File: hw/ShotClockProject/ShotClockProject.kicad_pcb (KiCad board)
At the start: 2 copper layers, 94 parts, among them IC1 TP4056-42-ESOP8_Rearanged, J1 USB_C_Receptacle_USB2.0, J10 Conn_01x33_Pin, J2 Conn_ST_STDC14, J3 Conn_01x06_Pin, J4 Conn_01x03_Pin, J5 Conn_01x02_Pin, J6 Conn_01x03_Pin, J7 Conn_01x33_Pin, J8 Conn_01x33_Pin, J9 Conn_01x33_Pin, Q1 Q_NPN_BCE, Q2 Q_PMOS_SGD, SW1 SW_SPDT, SW2 SW_SPDT, SW3 SW_SPST, SW4 SW_SPST, SW5 SW_SPST, U1 STM32F103RCT6, U2 LD39015M33R, U3 TPS63000, U4 M74HC14YRM13TR, Y1 16MHz

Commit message: Changed footprint
To horizontal 2.54 connectors
and started on rough layout
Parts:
- C10, C11, C12, C13, C15, C17, C2, C21, C22, C23, C24, C3, C4, C5, C6, C7, C8, C9: footprint Capacitor_SMD:C_0603_1608Metric -> Capacitor_SMD:C_0402_1005Metric
- J2: footprint Connector_PinHeader_1.27mm:PinHeader_2x07_P1.27mm_Vertical_SMD -> Connector_PinHeader_1.27mm:PinHeader_2x07_P1.27mm_Horizontal
- J3: footprint Connector_PinHeader_2.54mm:PinHeader_1x06_P2.54mm_Vertical_SMD_Pin1Left -> Connector_PinHeader_2.54mm:PinHeader_1x06_P2.54mm_Horizontal
- J4: footprint Connector_PinHeader_1.00mm:PinHeader_1x03_P1.00mm_Vertical_SMD_Pin1Left -> Connector_PinHeader_1.00mm:PinHeader_1x03_P1.00mm_Horizontal
- J5: footprint Connector_PinHeader_2.54mm:PinHeader_1x02_P2.54mm_Vertical_SMD_Pin1Left -> Connector_PinHeader_2.54mm:PinHeader_1x02_P2.54mm_Horizontal
- J6: footprint Connector_PinHeader_2.54mm:PinHeader_1x03_P2.54mm_Vertical_SMD_Pin1Left -> Connector_PinHeader_2.54mm:PinHeader_1x03_P2.54mm_Horizontal
- R1, R10, R11, R12, R13, R14, R15, R16, R17, R18, R19, R2, R20, R21, R22, R23, R24, R25, R26, R27, R3, R4, R5, R6, R7, R8, R9: footprint Resistor_SMD:R_0603_1608Metric -> Resistor_SMD:R_0402_1005Metric
- moved J9 121.1 mm to (186.8, 156.8), turned to -90 degrees
- moved J10 111.9 mm to (100.8, 152.5), turned to 180 degrees
- moved Y1 111.3 mm to (134.3, 93.7)
- moved C10 110.3 mm to (137.2, 93.1), turned to 90 degrees
- moved C11 110.2 mm to (137.2, 95.1), turned to 90 degrees
- moved C7 108.6 mm to (139.7, 97.5)
- moved C2 108.4 mm to (143.9, 88.0)
- moved FB1 108.2 mm to (138.2, 103.8)
- moved J1 108.1 mm to (168.9, 94.9)
- moved R3 108.1 mm to (161.9, 96.5)
- moved R5 108.1 mm to (161.9, 98.5)
- moved R6 108.1 mm to (161.7, 93.5)
- moved U1 108.1 mm to (147.5, 95.6)
- moved C4 107.9 mm to (144.5, 103.5)
- moved C5 107.4 mm to (151.2, 103.5)
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
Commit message: Added manufacturer folders
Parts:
- moved R1 153.5 mm to (125.5, 78.8), turned to 90 degrees
- moved IC1 144.8 mm to (118.2, 124.2), turned to 90 degrees
- moved R4 131.5 mm to (145.8, 87.5), turned to -90 degrees
- moved SW2 124.0 mm to (146.0, 82.5), turned to 180 degrees
- moved Q2 120.5 mm to (151.7, 113.2), turned to -90 degrees
- moved R11 104.0 mm to (158.2, 98.0)
- moved J2 63.4 mm to (158.2, 77.4), turned to 0 degrees
- moved J3 28.1 mm to (169.8, 104.8)
- moved SW1 13.2 mm to (126.2, 73.5)

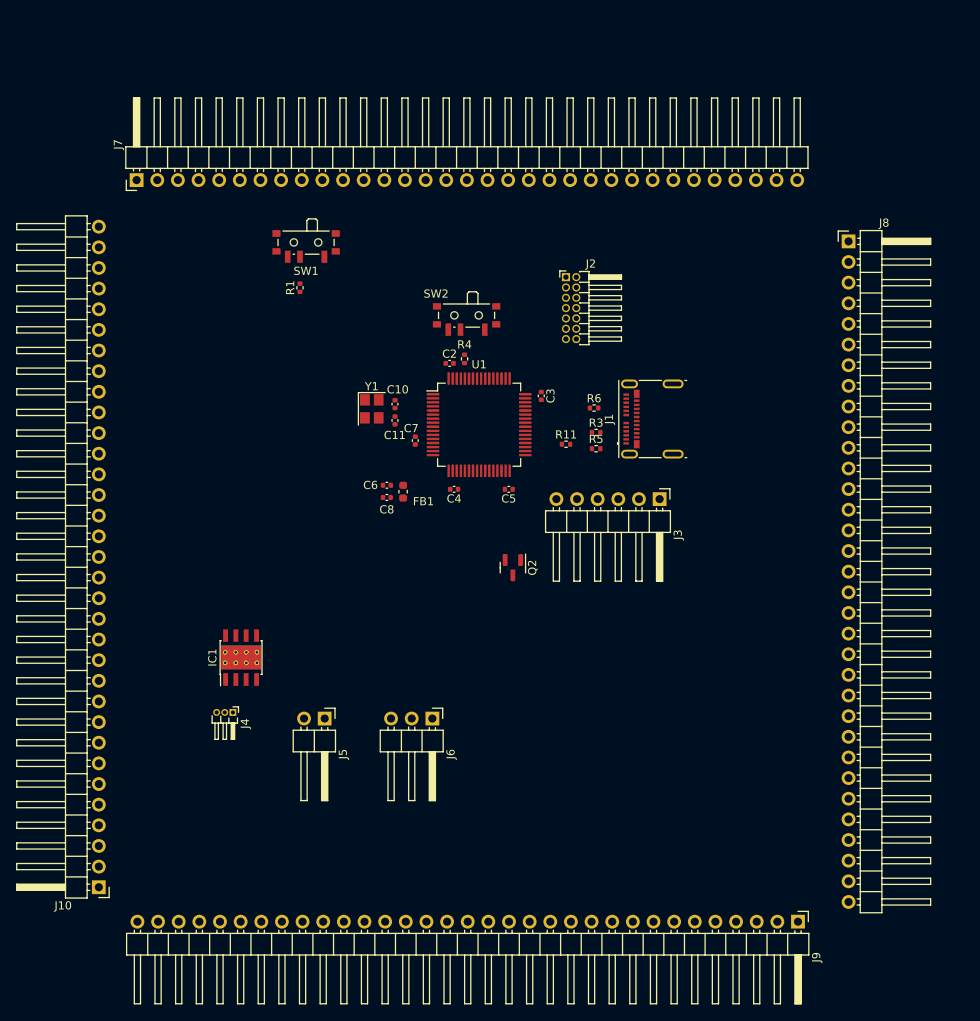
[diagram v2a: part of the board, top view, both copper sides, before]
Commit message: Changes headers, usb schematic and footprint
Now using standing USBc
Header & header pins are imported
All have 3d models now.

Removed fp-info-cache and added it to gitignore
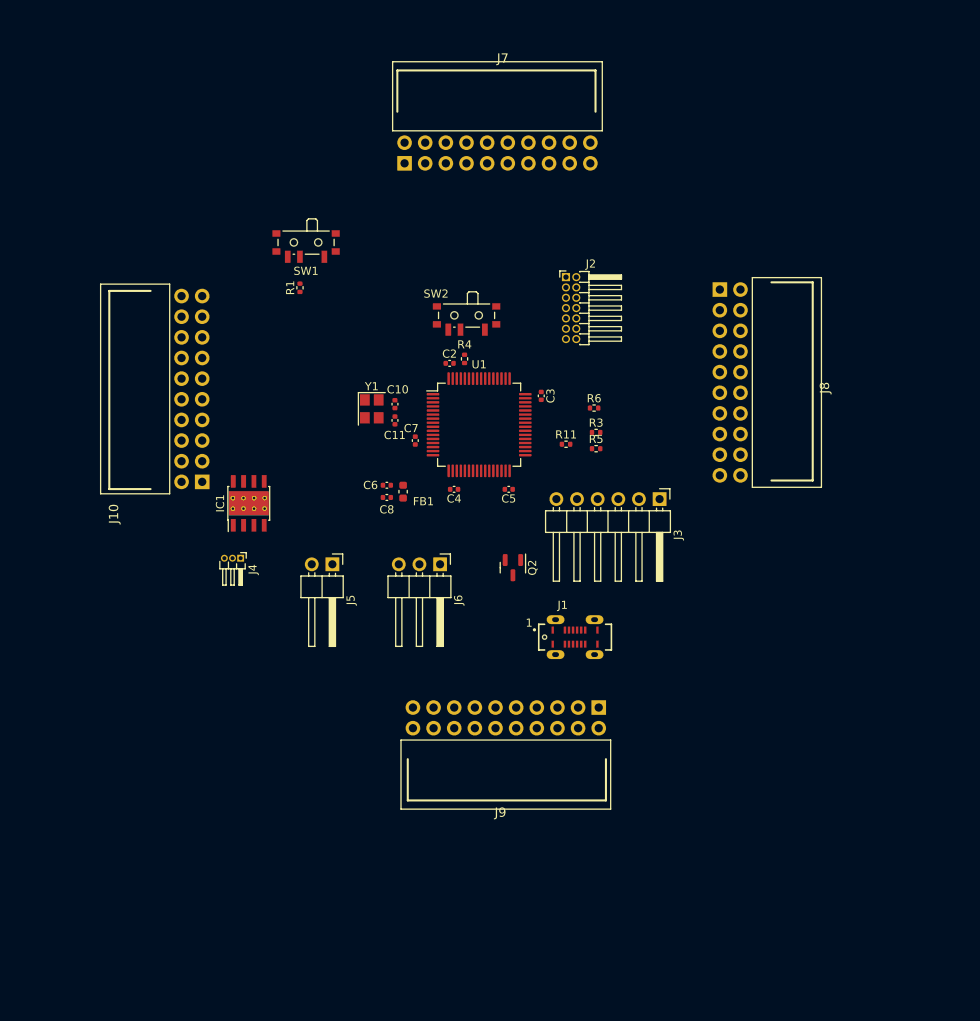
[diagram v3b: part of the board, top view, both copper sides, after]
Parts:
- J1: value USB_C_Receptacle_USB2.0 -> USB4120-03-C_REVA; footprint Connector_USB:USB_C_Receptacle_Molex_105450-0101 -> USB4120-03-C:GCT_USB4120-03-C_REVA_With3DModel
- J10, J7, J8, J9: value Conn_01x33_Pin -> DW254W-22-20-85; footprint Connector_PinHeader_2.54mm:PinHeader_1x33_P2.54mm_Horizontal -> DW254W-22-20-85:CONN-TH_20P-P2.54_DEALON_DW254W-22-20-85
- moved J10 62.4 mm to (112.2, 91.2), turned to 90 degrees
- moved J7 44.5 mm to (149.8, 62.2), turned to 0 degrees
- moved J9 43.8 mm to (150.8, 131.7), turned to 180 degrees
- moved J1 28.5 mm to (159.3, 121.7), turned to 0 degrees
- moved J8 22.7 mm to (178.4, 90.4), turned to -90 degrees
- moved IC1 19.0 mm to (119.2, 105.3)
- moved J4 19.0 mm to (118.2, 112.0)
- moved J5 19.0 mm to (129.5, 112.8)
- moved J6 19.0 mm to (142.7, 112.8)
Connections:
- J10 pad 10: /Connectors to segment displays/PWM5_TIM3_CH1 -> /Connectors to segment displays/PWM12_TIM4_CH4
- J10 pad 11: GND -> /Connectors to segment displays/PWM5_TIM3_CH1
- J10 pad 12: /Connectors to segment displays/PWM6_TIM3_CH2 -> /Connectors to segment displays/PWM13_TIM5_CH1
- J10 pad 13: GND -> /Connectors to segment displays/PWM6_TIM3_CH2
- J10 pad 14: /Connectors to segment displays/PWM7_TIM3_CH3 -> /Connectors to segment displays/PWM14_TIM5_CH2
- J10 pad 15: GND -> /Connectors to segment displays/PWM7_TIM3_CH3
- J10 pad 16: /Connectors to segment displays/PWM8_TIM3_CH4 -> /Connectors to segment displays/PWM15_TIM5_CH3
- J10 pad 17: GND -> /Connectors to segment displays/PWM8_TIM3_CH4
- J10 pad 18: /Connectors to segment displays/PWM9_TIM4_CH1 -> /Connectors to segment displays/PWM16_TIM5_CH4
- J10 pad 2: /Connectors to segment displays/PWM1_TIM2_CH1 -> GND
- J10 pad 20: /Connectors to segment displays/PWM10_TIM4_CH2 -> GND
- J10 pad 3: GND -> /Connectors to segment displays/PWM1_TIM2_CH1
- J10 pad 4: /Connectors to segment displays/PWM2_TIM2_CH2 -> /Connectors to segment displays/PWM9_TIM4_CH1
- J10 pad 5: GND -> /Connectors to segment displays/PWM2_TIM2_CH2
- J10 pad 6: /Connectors to segment displays/PWM3_TIM2_CH3 -> /Connectors to segment displays/PWM10_TIM4_CH2
- J10 pad 7: GND -> /Connectors to segment displays/PWM3_TIM2_CH3
- J10 pad 8: /Connectors to segment displays/PWM4_TIM2_CH4 -> /Connectors to segment displays/PWM11_TIM4_CH3
- J10 pad 9: GND -> /Connectors to segment displays/PWM4_TIM2_CH4
- J7 pad 10: /Connectors to segment displays/PWM5_TIM3_CH1 -> /Connectors to segment displays/PWM12_TIM4_CH4
- J7 pad 11: GND -> /Connectors to segment displays/PWM5_TIM3_CH1
- J7 pad 12: /Connectors to segment displays/PWM6_TIM3_CH2 -> /Connectors to segment displays/PWM13_TIM5_CH1
- J7 pad 13: GND -> /Connectors to segment displays/PWM6_TIM3_CH2
- J7 pad 14: /Connectors to segment displays/PWM7_TIM3_CH3 -> /Connectors to segment displays/PWM14_TIM5_CH2
- J7 pad 15: GND -> /Connectors to segment displays/PWM7_TIM3_CH3
- J7 pad 16: /Connectors to segment displays/PWM8_TIM3_CH4 -> /Connectors to segment displays/PWM15_TIM5_CH3
- J7 pad 17: GND -> /Connectors to segment displays/PWM8_TIM3_CH4
- J7 pad 18: /Connectors to segment displays/PWM9_TIM4_CH1 -> /Connectors to segment displays/PWM16_TIM5_CH4
- J7 pad 2: /Connectors to segment displays/PWM1_TIM2_CH1 -> GND
- J7 pad 20: /Connectors to segment displays/PWM10_TIM4_CH2 -> GND
- J7 pad 3: GND -> /Connectors to segment displays/PWM1_TIM2_CH1
- J7 pad 4: /Connectors to segment displays/PWM2_TIM2_CH2 -> /Connectors to segment displays/PWM9_TIM4_CH1
- J7 pad 5: GND -> /Connectors to segment displays/PWM2_TIM2_CH2
- J7 pad 6: /Connectors to segment displays/PWM3_TIM2_CH3 -> /Connectors to segment displays/PWM10_TIM4_CH2
- J7 pad 7: GND -> /Connectors to segment displays/PWM3_TIM2_CH3
- J7 pad 8: /Connectors to segment displays/PWM4_TIM2_CH4 -> /Connectors to segment displays/PWM11_TIM4_CH3
- J7 pad 9: GND -> /Connectors to segment displays/PWM4_TIM2_CH4
- J8 pad 10: /Connectors to segment displays/PWM5_TIM3_CH1 -> /Connectors to segment displays/PWM12_TIM4_CH4
- J8 pad 11: GND -> /Connectors to segment displays/PWM5_TIM3_CH1
- J8 pad 12: /Connectors to segment displays/PWM6_TIM3_CH2 -> /Connectors to segment displays/PWM13_TIM5_CH1
- J8 pad 13: GND -> /Connectors to segment displays/PWM6_TIM3_CH2
- J8 pad 14: /Connectors to segment displays/PWM7_TIM3_CH3 -> /Connectors to segment displays/PWM14_TIM5_CH2
- J8 pad 15: GND -> /Connectors to segment displays/PWM7_TIM3_CH3
- J8 pad 16: /Connectors to segment displays/PWM8_TIM3_CH4 -> /Connectors to segment displays/PWM15_TIM5_CH3
- J8 pad 17: GND -> /Connectors to segment displays/PWM8_TIM3_CH4
- J8 pad 18: /Connectors to segment displays/PWM9_TIM4_CH1 -> /Connectors to segment displays/PWM16_TIM5_CH4
- J8 pad 2: /Connectors to segment displays/PWM1_TIM2_CH1 -> GND
- J8 pad 20: /Connectors to segment displays/PWM10_TIM4_CH2 -> GND
- J8 pad 3: GND -> /Connectors to segment displays/PWM1_TIM2_CH1
- J8 pad 4: /Connectors to segment displays/PWM2_TIM2_CH2 -> /Connectors to segment displays/PWM9_TIM4_CH1
- J8 pad 5: GND -> /Connectors to segment displays/PWM2_TIM2_CH2
- J8 pad 6: /Connectors to segment displays/PWM3_TIM2_CH3 -> /Connectors to segment displays/PWM10_TIM4_CH2
- J8 pad 7: GND -> /Connectors to segment displays/PWM3_TIM2_CH3
- J8 pad 8: /Connectors to segment displays/PWM4_TIM2_CH4 -> /Connectors to segment displays/PWM11_TIM4_CH3
- J8 pad 9: GND -> /Connectors to segment displays/PWM4_TIM2_CH4
- J9 pad 10: /Connectors to segment displays/PWM5_TIM3_CH1 -> /Connectors to segment displays/PWM12_TIM4_CH4
- J9 pad 11: GND -> /Connectors to segment displays/PWM5_TIM3_CH1
- J9 pad 12: /Connectors to segment displays/PWM6_TIM3_CH2 -> /Connectors to segment displays/PWM13_TIM5_CH1
- J9 pad 13: GND -> /Connectors to segment displays/PWM6_TIM3_CH2
- J9 pad 14: /Connectors to segment displays/PWM7_TIM3_CH3 -> /Connectors to segment displays/PWM14_TIM5_CH2
- J9 pad 15: GND -> /Connectors to segment displays/PWM7_TIM3_CH3
- J9 pad 16: /Connectors to segment displays/PWM8_TIM3_CH4 -> /Connectors to segment displays/PWM15_TIM5_CH3
- J9 pad 17: GND -> /Connectors to segment displays/PWM8_TIM3_CH4
- J9 pad 18: /Connectors to segment displays/PWM9_TIM4_CH1 -> /Connectors to segment displays/PWM16_TIM5_CH4
- J9 pad 2: /Connectors to segment displays/PWM1_TIM2_CH1 -> GND
- J9 pad 20: /Connectors to segment displays/PWM10_TIM4_CH2 -> GND
- J9 pad 3: GND -> /Connectors to segment displays/PWM1_TIM2_CH1
- J9 pad 4: /Connectors to segment displays/PWM2_TIM2_CH2 -> /Connectors to segment displays/PWM9_TIM4_CH1
- J9 pad 5: GND -> /Connectors to segment displays/PWM2_TIM2_CH2
- J9 pad 6: /Connectors to segment displays/PWM3_TIM2_CH3 -> /Connectors to segment displays/PWM10_TIM4_CH2
- J9 pad 7: GND -> /Connectors to segment displays/PWM3_TIM2_CH3
- J9 pad 8: /Connectors to segment displays/PWM4_TIM2_CH4 -> /Connectors to segment displays/PWM11_TIM4_CH3
- J9 pad 9: GND -> /Connectors to segment displays/PWM4_TIM2_CH4

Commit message: Changed locations
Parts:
- moved J3 51.1 mm to (211.5, 134.2)
- moved J8 46.4 mm to (224.8, 90.8)
- moved J6 35.6 mm to (118.9, 139.2)
- moved J5 30.7 mm to (103.7, 129.4)
- moved J4 23.8 mm to (95.4, 119.0)
- moved J1 18.1 mm to (163.2, 104.0)
- moved R6 15.6 mm to (164.0, 109.0), turned to -90 degrees
- moved R5 4.00 mm to (162.6, 94.6)
- moved R3 2.54 mm to (162.6, 99.0), turned to 90 degrees
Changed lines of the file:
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@@
   )
   (footprint "Resistor_SMD:R_0402_1005Metric" (layer "F.Cu")
-    (at 161.94 98.55)
+    (at 162.6 94.6)
     (descr "Resistor SMD 0402 (1005 Metric), square (rectangular) end terminal, IPC_7351 nominal, (Body size source: IPC-SM-782 page 72, https://www.pcb-3d.com/wordpress/wp-content/uploads/ipc-sm-782a_amendment_1_and_2.pdf), generated with kicad-footprint-generator")
     (tags "resistor")
@@
   )
   (footprint "Connector_PinHeader_2.54mm:PinHeader_1x06_P2.54mm_Horizontal" (layer "F.Cu")
-    (at 169.75 104.75 -90)
+    (at 211.48 134.2 -90)
     (descr "Through hole angled pin header, 1x06, 2.54mm pitch, 6mm pin length, single row")
     (tags "Through hole angled pin header THT 1x06 2.54mm single row")
@@
   )
   (footprint "Connector_PinHeader_2.54mm:PinHeader_1x02_P2.54mm_Horizontal" (layer "F.Cu")
-    (at 129.49 112.775 -90)
+    (at 103.74 129.4 -90)
     (descr "Through hole angled pin header, 1x02, 2.54mm pitch, 6mm pin length, single row")
     (tags "Through hole angled pin header THT 1x02 2.54mm single row")
@@
   )
   (footprint "Resistor_SMD:R_0402_1005Metric" (layer "F.Cu")
-    (at 161.94 96.55)
+    (at 162.6 99 90)
     (descr "Resistor SMD 0402 (1005 Metric), square (rectangular) end terminal, IPC_7351 nominal, (Body size source: IPC-SM-782 page 72, https://www.pcb-3d.com/wordpress/wp-content/uploads/ipc-sm-782a_amendment_1_and_2.pdf), generated with kicad-footprint-generator")
     (tags "resistor")
@@
     (property "ki_keywords" "R res resistor")
     (attr smd)
-    (fp_text reference "R3" (at 0 -1.17) (layer "F.SilkS")
-        (effects (font (size 1 1) (thickness 0.15)))
-    )
-    (fp_text value "5k1" (at 0 1.17) (layer "F.Fab")
-        (effects (font (size 1 1) (thickness 0.15)))
-    )
-    (fp_text user "${REFERENCE}" (at 0 0) (layer "F.Fab")
+    (fp_text reference "R3" (at 0 -1.17 90) (layer "F.SilkS")
+        (effects (font (size 1 1) (thickness 0.15)))
+    )
+    (fp_text value "5k1" (at 0 1.17 90) (layer "F.Fab")
+        (effects (font (size 1 1) (thickness 0.15)))
+    )
+    (fp_text user "${REFERENCE}" (at 0 0 90) (layer "F.Fab")
         (effects (font (size 0.26 0.26) (thickness 0.04)))
     )
@@
     (fp_line (start 0.525 0.27) (end -0.525 0.27)
       (stroke (width 0.1) (type solid)) (layer "F.Fab"))
-    (pad "1" smd roundrect (at -0.51 0) (size 0.54 0.64) (layers "F.Cu" "F.Paste" "F.Mask") (roundrect_rratio 0.25)
+    (pad "1" smd roundrect (at -0.51 0 90) (size 0.54 0.64) (layers "F.Cu" "F.Paste" "F.Mask") (roundrect_rratio 0.25)
       (net 110 "Net-(J1-CC1)") (pintype "passive"))
-    (pad "2" smd roundrect (at 0.51 0) (size 0.54 0.64) (layers "F.Cu" "F.Paste" "F.Mask") (roundrect_rratio 0.25)
+    (pad "2" smd roundrect (at 0.51 0 90) (size 0.54 0.64) (layers "F.Cu" "F.Paste" "F.Mask") (roundrect_rratio 0.25)
       (net 3 "GND") (pintype "passive"))
     (model "${KICAD6_3DMODEL_DIR}/Resistor_SMD.3dshapes/R_0402_1005Metric.wrl"
@@
   )
   (footprint "Connector_PinHeader_2.54mm:PinHeader_1x03_P2.54mm_Horizontal" (layer "F.Cu")
-    (at 142.74 112.775 -90)
+    (at 118.94 139.2 -90)
     (descr "Through hole angled pin header, 1x03, 2.54mm pitch, 6mm pin length, single row")
     (tags "Through hole angled pin header THT 1x03 2.54mm single row")
@@
   )
   (footprint "USB4120-03-C:GCT_USB4120-03-C_REVA_With3DModel" (layer "F.Cu")
-    (at 159.35 121.735)
+    (at 163.2 104)
     (property "MANUFACTURER" "GCT")
     (property "MAXIMUM_PACKAGE_HEIGHT" "6.5mm")
@@
     (property "Sheetname" "STM32F103RCT6")
     (attr smd)
-    (fp_text reference "J1" (at -1.524 -3.937) (layer "F.SilkS")
+    (fp_text reference "J1" (at -6.95 -1.735) (layer "F.SilkS")
         (effects (font (size 1 1) (thickness 0.15)))
     )
@@
   )
   (footprint "Resistor_SMD:R_0402_1005Metric" (layer "F.Cu")
-    (at 161.69 93.55)
+    (at 164 109 -90)
     (descr "Resistor SMD 0402 (1005 Metric), square (rectangular) end terminal, IPC_7351 nominal, (Body size source: IPC-SM-782 page 72, https://www.pcb-3d.com/wordpress/wp-content/uploads/ipc-sm-782a_amendment_1_and_2.pdf), generated with kicad-footprint-generator")
     (tags "resistor")
@@
     (property "ki_keywords" "R res resistor")
     (attr smd)
-    (fp_text reference "R6" (at 0 -1.17) (layer "F.SilkS")
-        (effects (font (size 1 1) (thickness 0.15)))
-    )
-    (fp_text value "5k1" (at 0 1.17) (layer "F.Fab")
-        (effects (font (size 1 1) (thickness 0.15)))
-    )
-    (fp_text user "${REFERENCE}" (at 0 0) (layer "F.Fab")
+    (fp_text reference "R6" (at 0 -1.17 90) (layer "F.SilkS")
+        (effects (font (size 1 1) (thickness 0.15)))
+    )
+    (fp_text value "5k1" (at 0 1.17 90) (layer "F.Fab")
+        (effects (font (size 1 1) (thickness 0.15)))
+    )
+    (fp_text user "${REFERENCE}" (at 0 0 90) (layer "F.Fab")
         (effects (font (size 0.26 0.26) (thickness 0.04)))
     )
@@
     (fp_line (start 0.525 0.27) (end -0.525 0.27)
       (stroke (width 0.1) (type solid)) (layer "F.Fab"))
-    (pad "1" smd roundrect (at -0.51 0) (size 0.54 0.64) (layers "F.Cu" "F.Paste" "F.Mask") (roundrect_rratio 0.25)
+    (pad "1" smd roundrect (at -0.51 0 270) (size 0.54 0.64) (layers "F.Cu" "F.Paste" "F.Mask") (roundrect_rratio 0.25)
       (net 111 "Net-(J1-CC2)") (pintype "passive"))
-    (pad "2" smd roundrect (at 0.51 0) (size 0.54 0.64) (layers "F.Cu" "F.Paste" "F.Mask") (roundrect_rratio 0.25)
+    (pad "2" smd roundrect (at 0.51 0 270) (size 0.54 0.64) (layers "F.Cu" "F.Paste" "F.Mask") (roundrect_rratio 0.25)
       (net 3 "GND") (pintype "passive"))
     (model "${KICAD6_3DMODEL_DIR}/Resistor_SMD.3dshapes/R_0402_1005Metric.wrl"
@@
   )
   (footprint "DW254W-22-20-85:CONN-TH_20P-P2.54_DEALON_DW254W-22-20-85" (layer "F.Cu")
-    (at 178.4325 90.4 -90)
+    (at 224.8325 90.8 -90)
     (property "JLC Part" "Extended Part")
     (property "LCSC Part" "C2936006")
@@
   )
   (footprint "Connector_PinHeader_1.00mm:PinHeader_1x03_P1.00mm_Horizontal" (layer "F.Cu")
-    (at 118.2 112.025 -90)
+    (at 95.4 119 -90)
     (descr "Through hole angled pin header, 1x03, 1.00mm pitch, 2.0mm pin length, single row")
     (tags "Through hole angled pin header THT 1x03 1.00mm single row")
